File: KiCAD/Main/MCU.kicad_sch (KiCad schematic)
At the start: 9 parts, among them U1 STM32H730VBTx

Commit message: Keep up to date
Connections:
- net +3V3: now also U1.6 (VBAT)
- net Camera User BTN: no longer U1.90 (PB4(NJTRST))
- net GPS SCL: now reaches U1.59 (PD12)
- net GPS SDA: now reaches U1.60 (PD13)
- net GPS_RX: no longer names the net of U1.22 (PA0)
- net GPS_TX: no longer names the net of U1.23 (PA1)
- net SD_RESET: no longer names the net of U1.79 (PC11)
- net Thermistor 1 renamed Drogue Eject Main
- net Thermistor 2 renamed Drogue Eject Backup
- net Thermistor 3 renamed Main Eject
- net Thermistor 4: no longer names the net of U1.18 (PC3_C)
- new net SD_MISO: U1.90 (PB4(NJTRST))

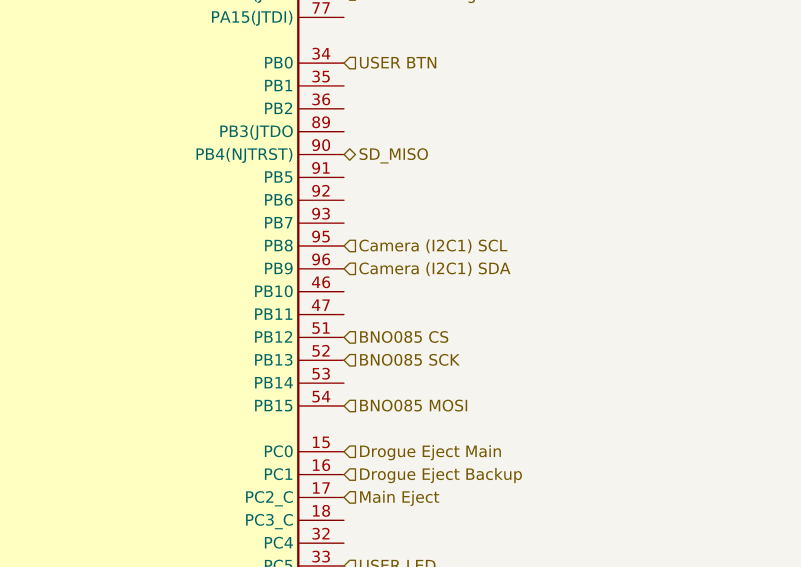
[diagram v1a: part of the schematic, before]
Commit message: Add datasheets and revise TMR goals
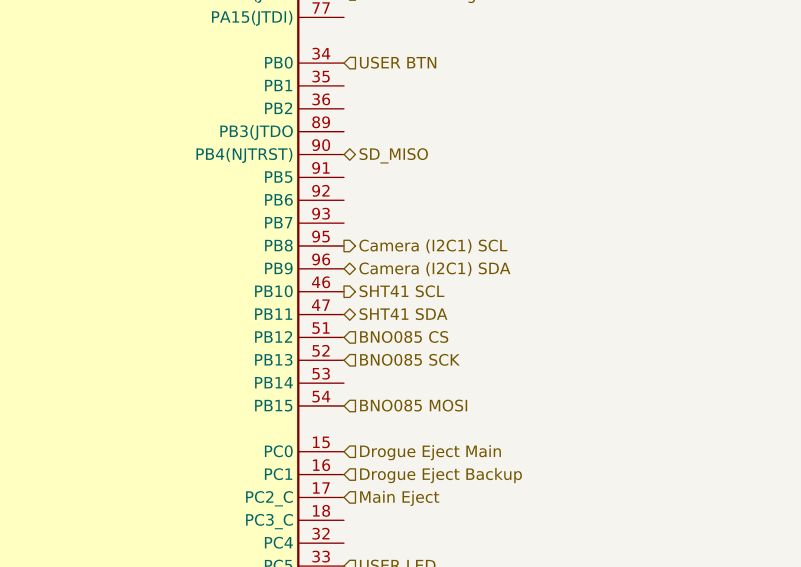
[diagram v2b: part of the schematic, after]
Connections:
- net SHT41 SCL: now reaches U1.46 (PB10)
- net SHT41 SDA: now reaches U1.47 (PB11)

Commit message: Polish for review
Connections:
- net BMP390 INT1: now reaches U1.1 (PE2)
- net BMP390 INT2: now reaches U1.2 (PE3)
- net SD MOSI: now reaches U1.31 (PA7)
- net SIMU CS3: now reaches U1.35 (PB1)
- net SIMU MOSI: now reaches U1.36 (PB2)
- net BNO085 MISO: now reaches U1.53 (PB14)
- net SIMU2 INT: now reaches U1.68 (PA9)
- net SIMU1 INT: now reaches U1.69 (PA10)
- net Radio TX: now reaches U1.78 (PC10)
- net SIMU MISO: now reaches U1.79 (PC11)
- net Radio AUX: now reaches U1.80 (PC12)
- net Radio RST: now reaches U1.81 (PD0)
- net SIMU CLK: now reaches U1.89 (PB3(JTDO)
- net Camera (I2C1) SCL renamed Radio RX
- net Camera (I2C1) SDA: no longer names the net of U1.96 (PB9)
- net Camera DCMI D0: no longer names the net of U1.63 (PC6)
- net Camera DCMI D1: no longer names the net of U1.64 (PC7)
- net Camera DCMI D2 renamed BNO085 INT
- net Camera DCMI D3 renamed BNO085 RST
- net Camera DCMI D4 renamed BMP390 INT3
- net Camera DCMI D5: no longer names the net of U1.84 (PD3)
- net Camera DCMI D6: no longer names the net of U1.4 (PE5)
- net Camera DCMI D7: no longer names the net of U1.5 (PE6)
- net Camera DCMI HSYNC renamed SD CS
- net Camera Debug SWCLK: no longer names the net of U1.76 (PA14(JTCK)
- net Camera Debug SWDIO: no longer names the net of U1.72 (PA13(JTMS)
- net Camera PWDN: no longer names the net of U1.61 (PD14)
- net Camera RCC MCO1 renamed SIMU3 INT
- net Camera RCC OSC IN: no longer names the net of U1.12 (PH0)
- net Camera RCC OSC OUT: no longer names the net of U1.13 (PH1)
- net Camera RCC OSC32 IN: no longer names the net of U1.8 (PC14)
- net Camera RCC OSC32 OUT: no longer names the net of U1.9 (PC15)
- net Camera RX renamed SIMU CS1
- net Camera Reset: no longer names the net of U1.62 (PD15)
- net Camera TX renamed SIMU CS2
- net Camera User BTN: no longer names the net of U1.7 (PC13)
- net SHT41 (SPI4) CS1: no longer names the net of U1.39 (PE9)
- net SHT41 (SPI4) CS2: no longer names the net of U1.40 (PE10)
- net SHT41 (SPI4) CS3: no longer names the net of U1.41 (PE11)
- net SHT41 and BMP390 (SPI4) MISO renamed BMP390 (SPI4) MISO
- net SHT41 and BMP390 (SPI4) MOSI renamed BMP390 (SPI4) MOSI
- net SHT41 and BMP390 (SPI4) SCK renamed BMP390 (SPI4) SCK

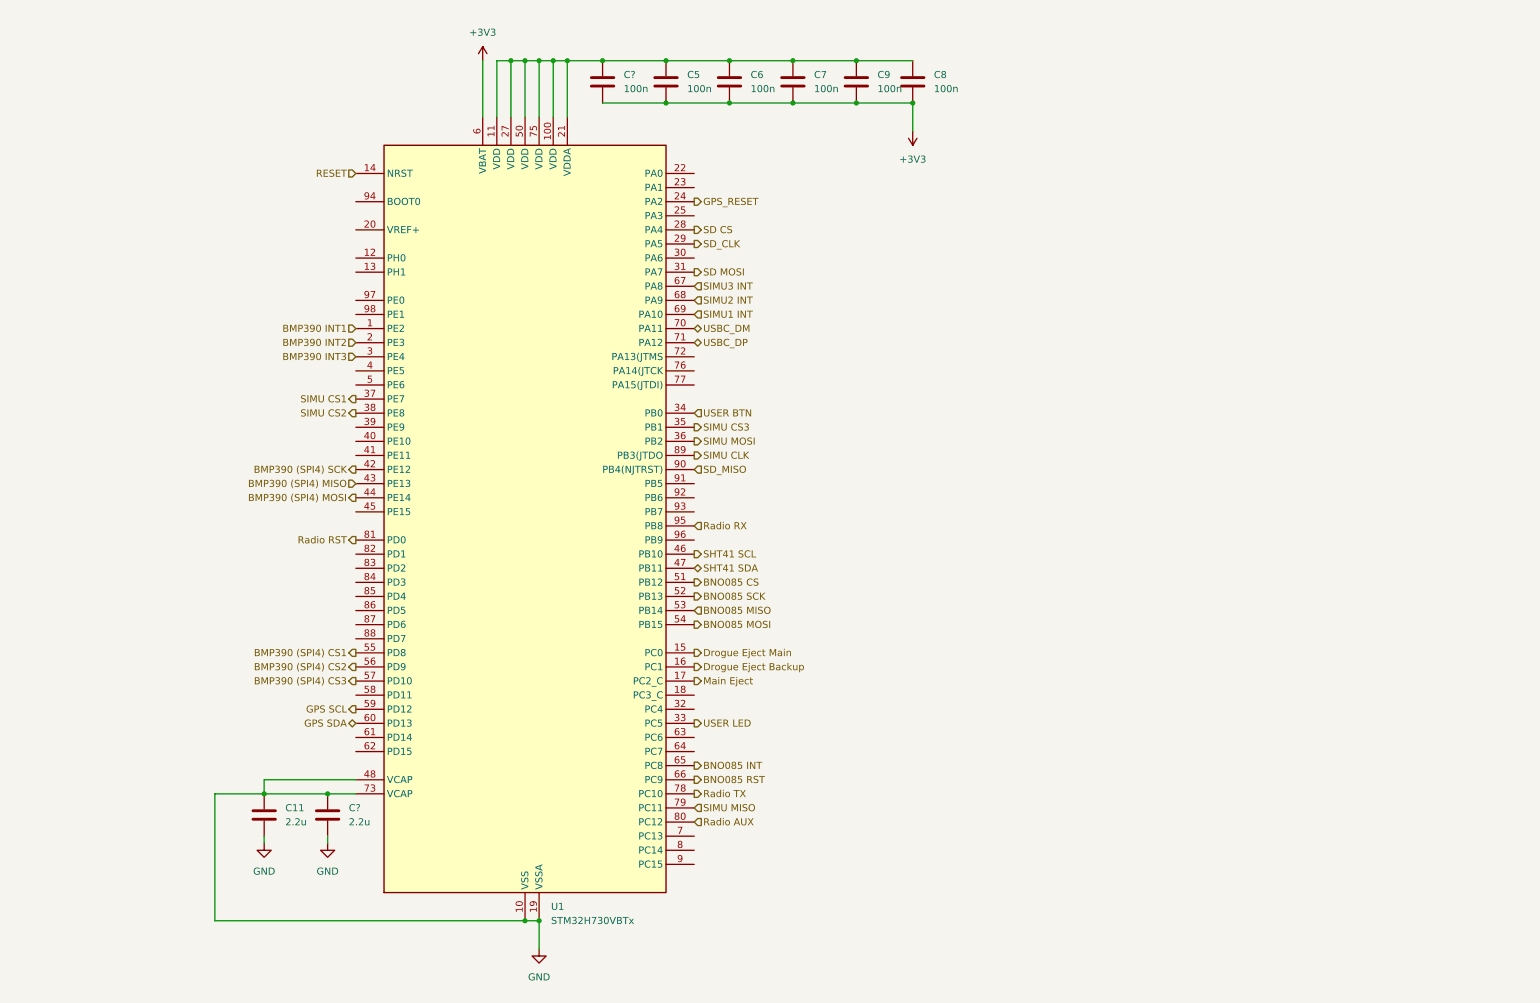
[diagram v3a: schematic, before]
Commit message: Create wiring diagram draft
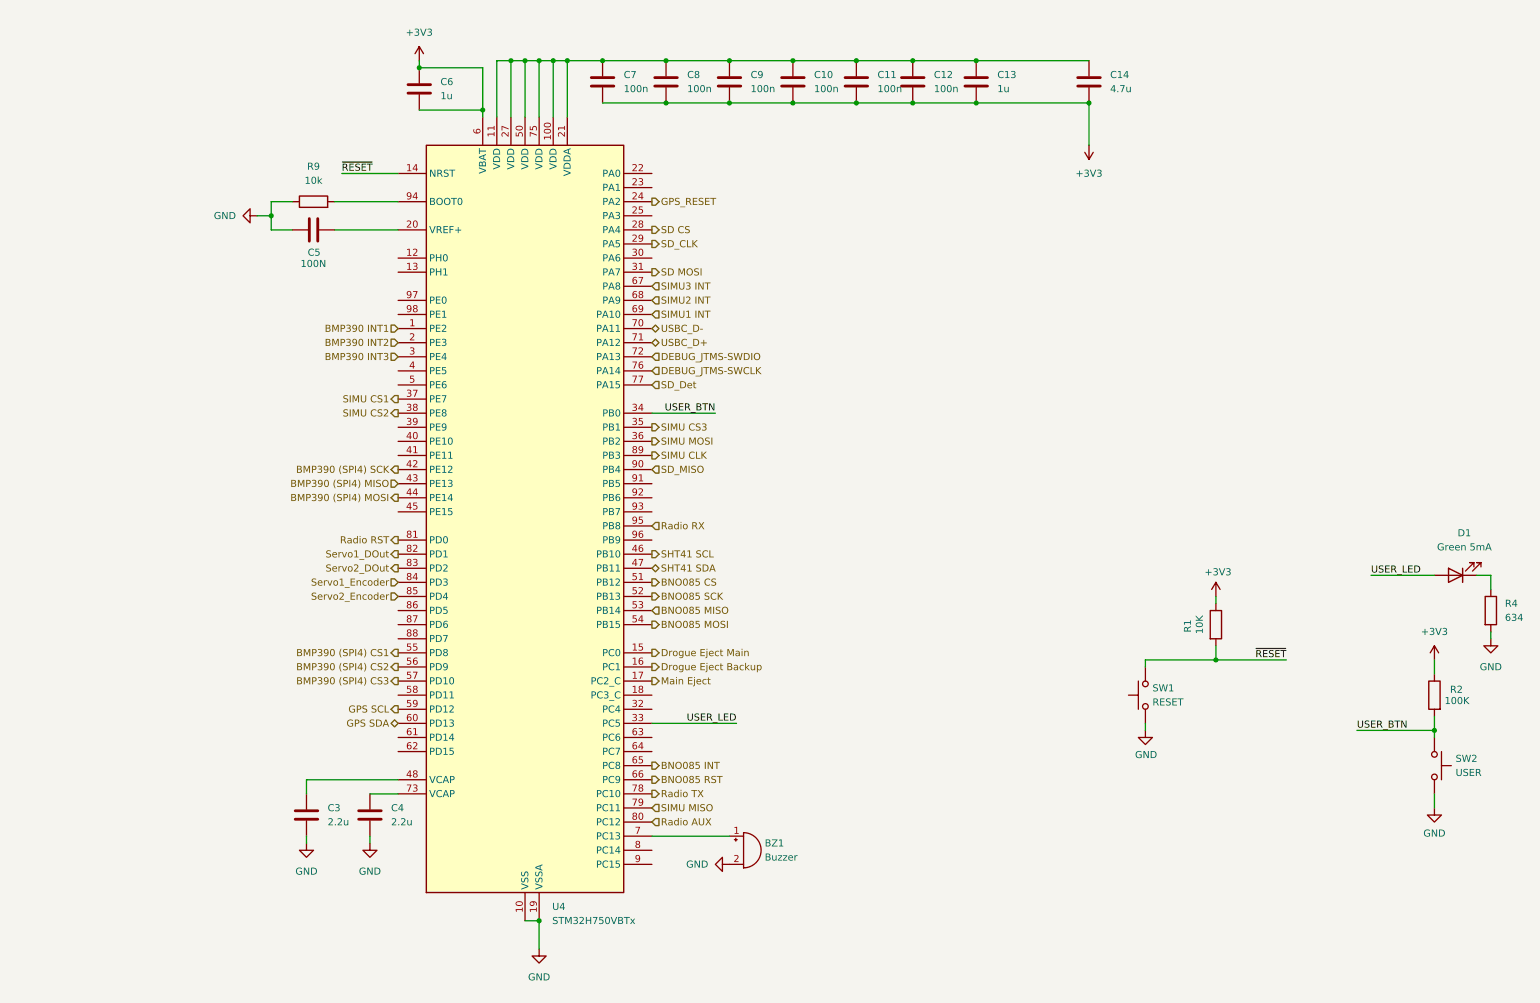
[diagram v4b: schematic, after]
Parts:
- removed U1: STM32H730VBTx, Package_QFP:LQFP-100_14x14mm_P0.5mm, symbol MCU_ST_STM32H7:STM32H730VBTx
- added BZ1: Buzzer, symbol Device:Buzzer
- added C13, C6: 1u, symbol Device:C
- added C14: 4.7u, symbol Device:C
- added C5: 100N, symbol Device:C
- added D1: Green 5mA, LED_SMD:LED_0603_1608Metric, symbol Device:LED
- added R1: 10K, Resistor_SMD:R_0603_1608Metric, symbol Device:R
- added R2: 100K, Resistor_SMD:R_0603_1608Metric, symbol Device:R
- added R4: 634, Resistor_SMD:R_0603_1608Metric, symbol Device:R
- added R9: 10k, symbol Device:R
- added SW1: RESET, Button_Switch_SMD:SW_Push_1P1T_NO_Vertical_Wuerth_434133025816, symbol Switch:SW_Push
- added SW2: USER, Button_Switch_SMD:SW_Push_1P1T_NO_Vertical_Wuerth_434133025816, symbol Switch:SW_Push
- added U4: STM32H750VBTx, Package_QFP:LQFP-100_14x14mm_P0.5mm, symbol MCU_ST_STM32H7:STM32H750VBTx
- gave numbers to parts that had none: 2
- renumbered C7 to C10, C9 to C11, C8 to C12, C11 to C3, C5 to C8, C6 to C9
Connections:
- net +3V3: now also C13.2, C14.2, C6.1, C6.2, R1.1, R2.1, U4.6 (VBAT)
- net BMP390 (SPI4) CS1: now also U4.55 (PD8)
- net BMP390 (SPI4) CS2: now also U4.56 (PD9)
- net BMP390 (SPI4) CS3: now also U4.57 (PD10)
- net BMP390 (SPI4) MISO: now also U4.43 (PE13)
- net BMP390 (SPI4) MOSI: now also U4.44 (PE14)
- net BMP390 (SPI4) SCK: now also U4.42 (PE12)
- net BMP390 INT1: now also U4.1 (PE2)
- net BMP390 INT2: now also U4.2 (PE3)
- net BMP390 INT3: now also U4.3 (PE4)
- net BNO085 CS: now also U4.51 (PB12)
- net BNO085 INT: now also U4.65 (PC8)
- net BNO085 MISO: now also U4.53 (PB14)
- net BNO085 MOSI: now also U4.54 (PB15)
- net BNO085 RST: now also U4.66 (PC9)
- net BNO085 SCK: now also U4.52 (PB13)
- net Drogue Eject Backup: now also U4.16 (PC1)
- net Drogue Eject Main: now also U4.15 (PC0)
- net GND: now also BZ1.2 (-), C5.1, R4.2, R9.1, SW1.1, SW2.1, U4.10 (VSS), U4.19 (VSSA), U4.26 (VSS), U4.49 (VSS), U4.74 (VSS), U4.99 (VSS); no longer C3.1, C4.1
- net GPS SCL: now also U4.59 (PD12)
- net GPS SDA: now also U4.60 (PD13)
- net GPS_RESET: now also U4.24 (PA2)
- net Main Eject: now also U4.17 (PC2_C)
- net Radio AUX: now also U4.80 (PC12)
- net Radio RST: now also U4.81 (PD0)
- net Radio RX: now also U4.95 (PB8)
- net Radio TX: now also U4.78 (PC10)
- net SD CS: now also U4.28 (PA4)
- net SD MOSI: now also U4.31 (PA7)
- net SD_CLK: now also U4.29 (PA5)
- net SD_MISO: now also U4.90 (PB4)
- net SHT41 SCL: now also U4.46 (PB10)
- net SHT41 SDA: now also U4.47 (PB11)
- net SIMU CLK: now also U4.89 (PB3)
- net SIMU CS1: now also U4.37 (PE7)
- net SIMU CS2: now also U4.38 (PE8)
- net SIMU CS3: now also U4.35 (PB1)
- net SIMU MISO: now also U4.79 (PC11)
- net SIMU MOSI: now also U4.36 (PB2)
- net SIMU1 INT: now also U4.69 (PA10)
- net SIMU2 INT: now also U4.68 (PA9)
- net SIMU3 INT: now also U4.67 (PA8)
- net at C10.1, C11.1, C12.1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: now also C13.1, C14.1, U4.100 (VDD), U4.11 (VDD), U4.21 (VDDA), U4.27 (VDD), U4.50 (VDD), U4.75 (VDD)
- new net: D1.1 (K), R4.1
- new net: C5.2, U4.20 (VREF+)
- new net: C3.1, U4.48 (VCAP)
- new net: BZ1.1 (+), U4.7 (PC13)
- new net: C4.1, U4.73 (VCAP)
- new net: R9.2, U4.94 (BOOT0)
- new net DEBUG_JTMS-SWCLK: U4.76 (PA14)
- new net DEBUG_JTMS-SWDIO: U4.72 (PA13)
- new net SD_Det: U4.77 (PA15)
- new net Servo1_DOut: U4.82 (PD1)
- new net Servo1_Encoder: U4.84 (PD3)
- new net Servo2_DOut: U4.83 (PD2)
- new net Servo2_Encoder: U4.85 (PD4)
- new net USBC_D+: U4.71 (PA12)
- new net USBC_D-: U4.70 (PA11)
- new net USER_BTN: R2.2, SW2.2, U4.34 (PB0)
- new net USER_LED: D1.2 (A), U4.33 (PC5)
- new net ~{RESET}: R1.2, SW1.2, U4.14 (NRST)
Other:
- moved on the sheet: C3, C4

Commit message: Submit design for review
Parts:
- added C36: 0.1u, symbol Device:C
- added C37: 15p, symbol Device:C
- added R29: 1k, symbol Device:R
- added Y2: SiT8008xx-2x-xxE, Oscillator:Oscillator_SMD_SiT_PQFN-4Pin_3.2x2.5mm, symbol Oscillator:SiT8008xx-2x-xxE
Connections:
- net +3V3: now also C36.2, R29.1, Y2.4 (Vdd)
- net GND: now also C36.1, C37.1, Y2.2 (GND)
- net ~{OSC_OUT}: now reaches U4.12 (PH0)
- net ~{OSC_OUT}: now also C37.2, Y2.3 (OUT)
- net BNO085 RST: no longer names the net of U4.66 (PC9)
- new net: R29.2, Y2.1 (OE)

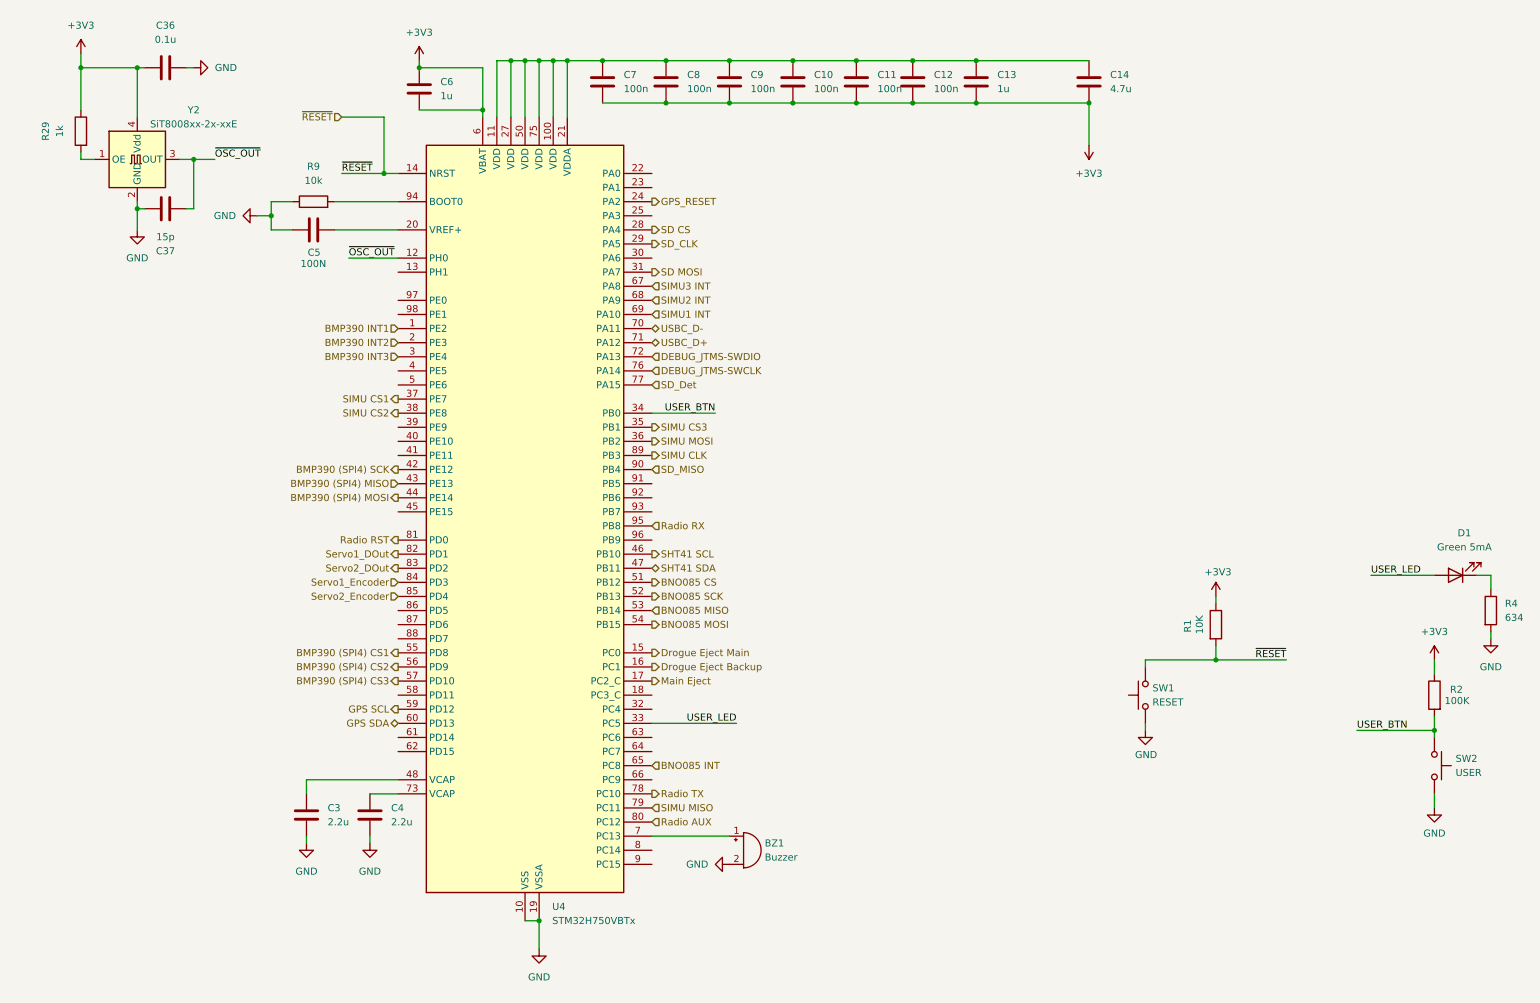
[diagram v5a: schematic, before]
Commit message: Update RF sys and footprints
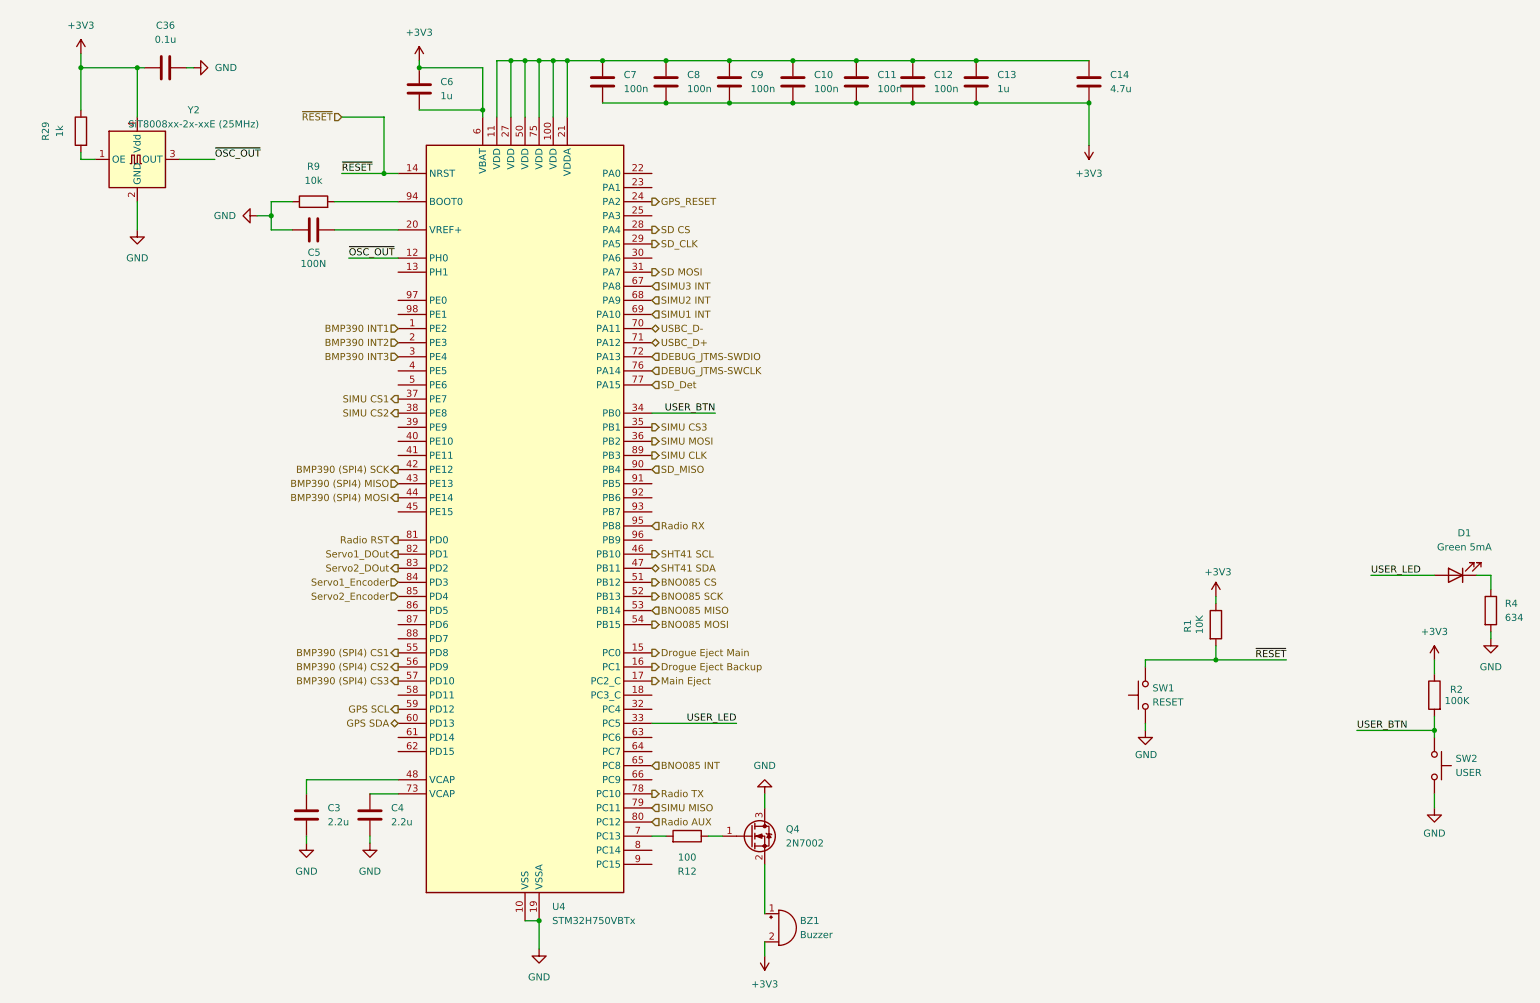
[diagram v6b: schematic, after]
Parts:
- removed C37: 15p, symbol Device:C
- added Q4: 2N7002, Package_TO_SOT_SMD:SOT-23, symbol Transistor_FET:2N7002
- added R12: 100, Resistor_SMD:R_0603_1608Metric, symbol Device:R
- BZ1: footprint (none) -> Buzzer_Beeper:MagneticBuzzer_PUI_SMT-1028-T-2-R
- C10, C11, C12, C13, C14, C3, C36, C4, C5, C6, C7, C8, C9: footprint (none) -> Capacitor_SMD:C_0603_1608Metric
- R29, R9: footprint (none) -> Resistor_SMD:R_0603_1608Metric
- Y2: value SiT8008xx-2x-xxE -> SiT8008xx-2x-xxE (25MHz)
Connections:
- net +3V3: now also BZ1.2 (-)
- net GND: now also Q4.3 (D); no longer BZ1.2 (-)
- net at U4.7 (PC13): now also R12.2; no longer BZ1.1 (+)
- new net: Q4.1 (G), R12.1
- new net: BZ1.1 (+), Q4.2 (S)
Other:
- moved on the sheet: BZ1

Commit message: 30%
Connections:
- net +3V3: now also C10.1, C11.1, C12.1, C13.1, C14.1, C7.1, C8.1, C9.1, U4.100 (VDD), U4.11 (VDD), U4.21 (VDDA), U4.27 (VDD), U4.50 (VDD), U4.75 (VDD); no longer C10.2, C11.2, C12.2, C13.2, C14.2, C6.1, C7.2, C8.2, C9.2
- net GND: now also C10.2, C11.2, C12.2, C13.2, C14.2, C6.1, C7.2, C8.2, C9.2
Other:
- moved on the sheet: C14, C6
